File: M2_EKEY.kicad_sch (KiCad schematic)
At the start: 42 parts, among them J2 Bus_M.2_Socket_E, J31 Bus_M.2_Socket_E, J34 Bus_M.2_Socket_E

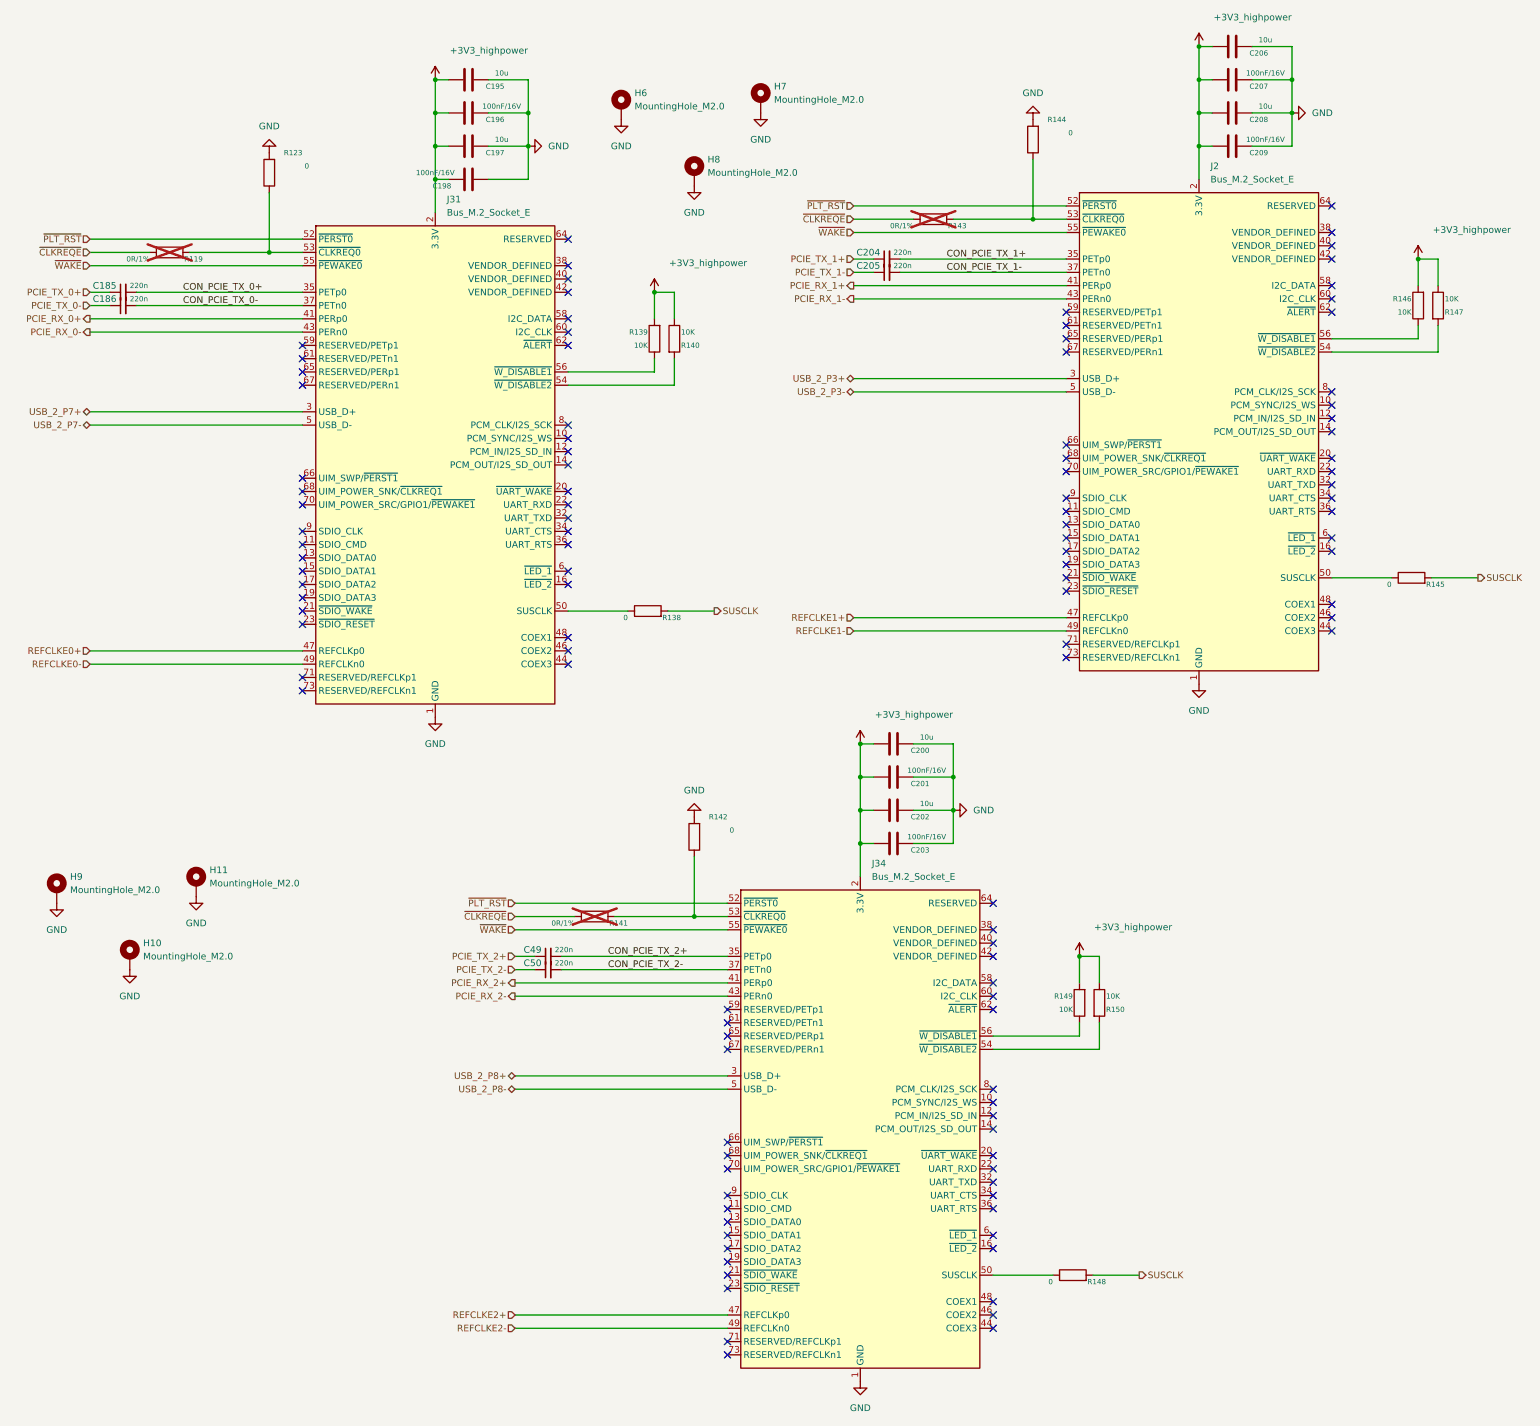
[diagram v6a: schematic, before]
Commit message: added MPN to all parts by hand :'(
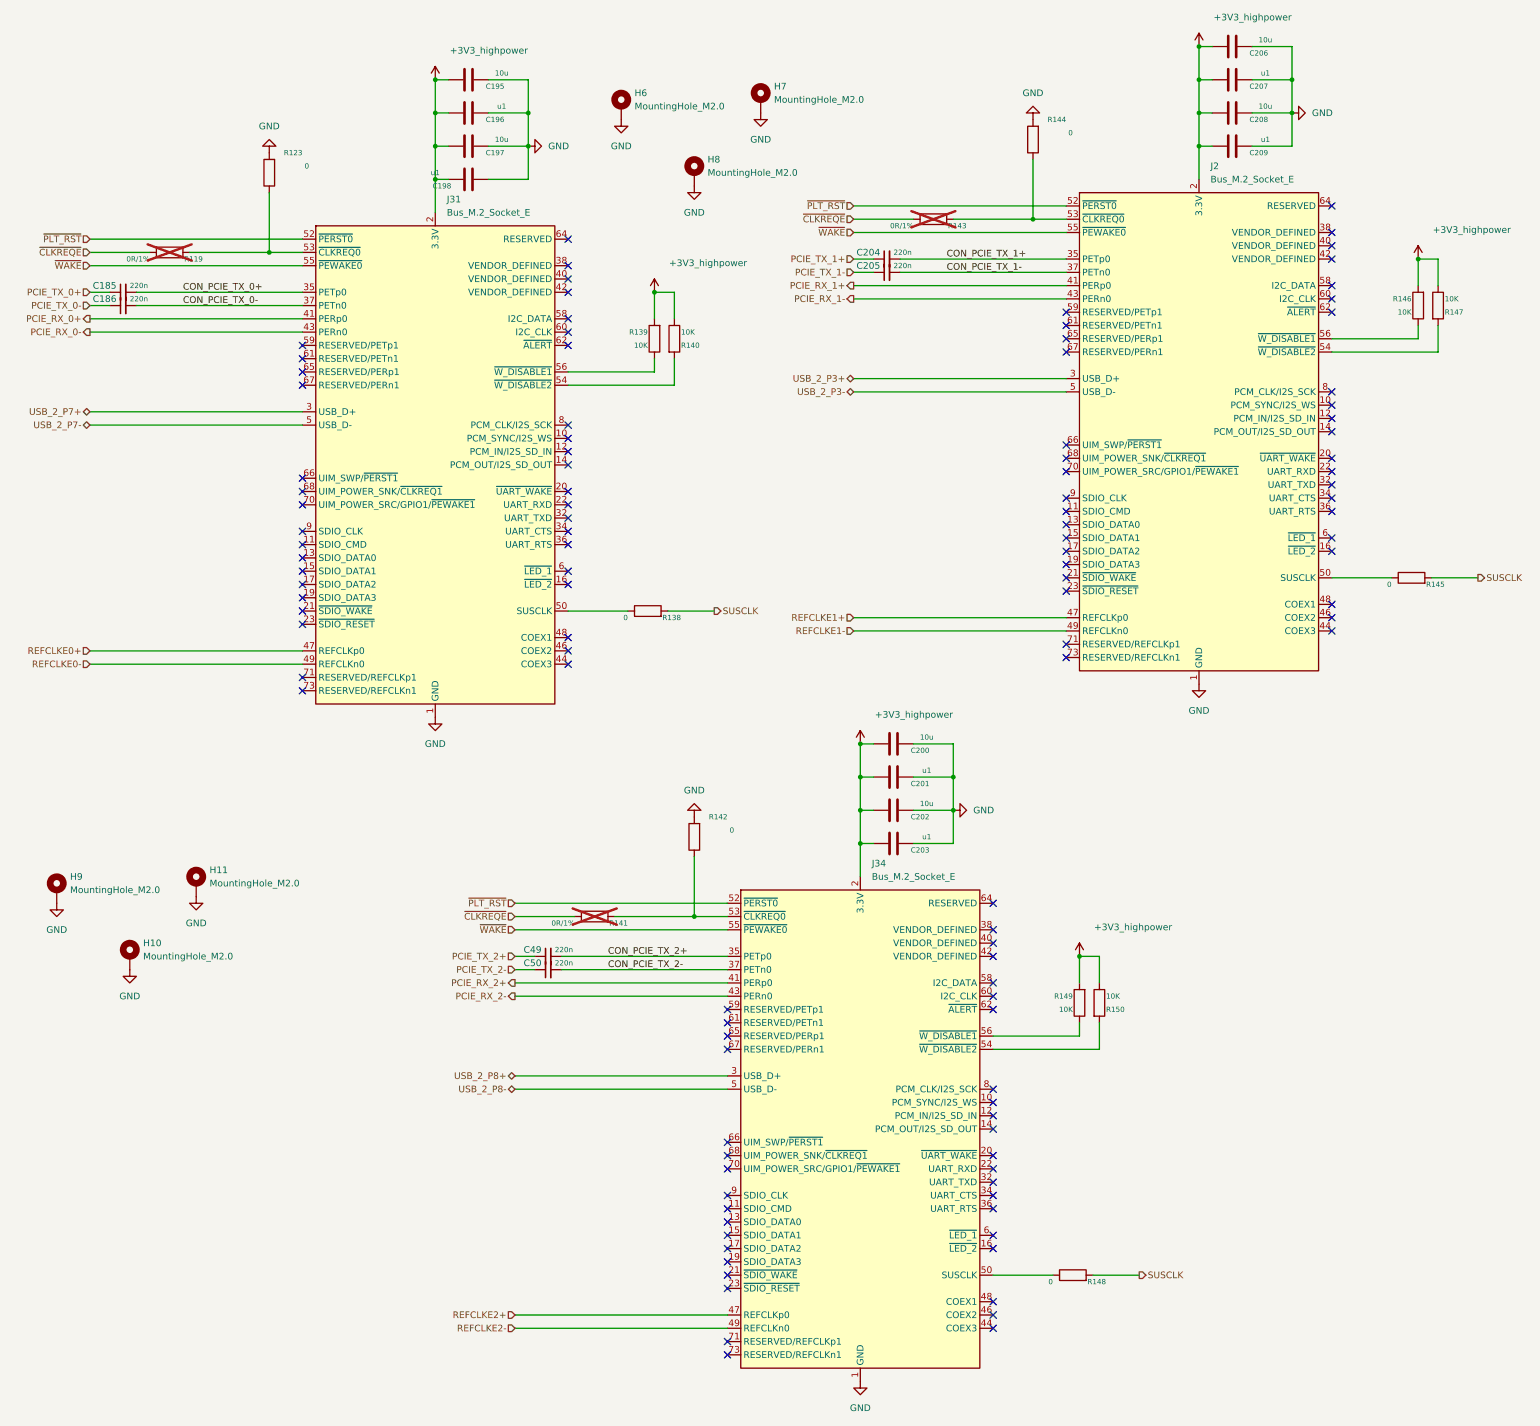
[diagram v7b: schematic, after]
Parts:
- C195, C197, C200, C202, C206, C208: footprint A_HDJ_Library:C_0402_1005Metric -> A_DFRobot:C_0603; DF_Comment 贴片电容0402-10UF-10V-X5R_GRM155R61A106ME44D -> (none); MPN MLASL168BB5106MTNB33 -> GRM188R61E106KA73D; SCH_Show_Footprint C0402 -> (none)
- C196: value 100nF/16V -> u1; MPN (none) -> C1005X7R1H104K050BE
- C198, C201, C203, C207, C209: value 100nF/16V -> u1; DF_Comment 贴片电容0402-100nF-16V-X7R(0402) -> (none); MPN (none) -> C1005X7R1H104K050BE
- J2, J31, J34: MPN (none) -> APCI0108-P001A
- R138, R145, R148: MPN C2889341 -> MCS0402HZ0000ZE100
- R139, R140, R146, R147, R149, R150: MPN RC0402FR-1310KL -> RCS040210K0FKED
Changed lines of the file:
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@@
 			)
 		)
-		(property "Value" "100nF/16V"
+		(property "Value" "u1"
 			(at 229.87 171.45 90)
 			(show_name no)
@@
 			)
 		)
-		(property "Description" ""
+		(property "Description" "16v"
 			(at 223.52 172.72 0)
 			(hide yes)
@@
 			)
 		)
-		(property "DF_Comment" "贴片电容0402-100nF-16V-X7R(0402)"
+		(property "DF_Comment" ""
 			(at 223.52 172.72 0)
 			(hide yes)
@@
 			)
 		)
-		(property "Field-1" ""
+		(property "MPN" "C1005X7R1H104K050BE"
 			(at 223.52 172.72 0)
 			(hide yes)
@@
 			)
 		)
-		(property "Value" "100nF/16V"
+		(property "Value" "u1"
 			(at 294.64 25.4 90)
 			(show_name no)
@@
 			)
 		)
-		(property "DF_Comment" "贴片电容0402-100nF-16V-X7R(0402)"
+		(property "DF_Comment" ""
 			(at 288.29 26.67 0)
 			(hide yes)
@@
 			)
 		)
-		(property "Field-1" ""
+		(property "MPN" "C1005X7R1H104K050BE"
 			(at 288.29 26.67 0)
 			(hide yes)
@@
 			)
 		)
-		(property "Value" "100nF/16V"
+		(property "Value" "u1"
 			(at 294.64 38.1 90)
 			(show_name no)
@@
 			)
 		)
-		(property "DF_Comment" "贴片电容0402-100nF-16V-X7R(0402)"
+		(property "DF_Comment" ""
 			(at 288.29 39.37 0)
 			(hide yes)
@@
 			)
 		)
-		(property "Field-1" ""
+		(property "MPN" "C1005X7R1H104K050BE"
 			(at 288.29 39.37 0)
 			(hide yes)
@@
 			)
 		)
-		(property "Footprint" "A_HDJ_Library:C_0402_1005Metric"
+		(property "Footprint" "A_DFRobot:C_0603"
 			(at 284.48 21.2852 0)
 			(hide yes)
@@
 			)
 		)
-		(property "DF_Comment" "贴片电容0402-10UF-10V-X5R_GRM155R61A106ME44D"
+		(property "DF_Comment" ""
 			(at 288.29 20.32 0)
 			(hide yes)
@@
 			)
 		)
-		(property "SCH_Show_Footprint" "C0402"
+		(property "SCH_Show_Footprint" ""
 			(at 288.29 20.32 0)
 			(hide yes)
@@
 			)
 		)
-		(property "MPN" "MLASL168BB5106MTNB33"
+		(property "MPN" "GRM188R61E106KA73D"
 			(at 288.29 20.32 0)
 			(hide yes)
@@
 			)
 		)
-		(property "Footprint" "A_HDJ_Library:C_0402_1005Metric"
+		(property "Footprint" "A_DFRobot:C_0603"
 			(at 138.43 27.6352 0)
 			(hide yes)
@@
 			)
 		)
-		(property "DF_Comment" "贴片电容0402-10UF-10V-X5R_GRM155R61A106ME44D"
+		(property "DF_Comment" ""
 			(at 142.24 26.67 0)
 			(hide yes)
@@
 			)
 		)
-		(property "SCH_Show_Footprint" "C0402"
+		(property "SCH_Show_Footprint" ""
 			(at 142.24 26.67 0)
 			(hide yes)
@@
 			)
 		)
-		(property "MPN" "MLASL168BB5106MTNB33"
+		(property "MPN" "GRM188R61E106KA73D"
 			(at 142.24 26.67 0)
 			(hide yes)
@@
 			)
 		)
-		(property "MPN" "C2889341"
+		(property "MPN" "MCS0402HZ0000ZE100"
 			(at 322.58 121.92 0)
 			(hide yes)
@@
 			)
 		)
-		(property "Value" "100nF/16V"
+		(property "Value" "u1"
 			(at 229.87 158.75 90)
 			(show_name no)
@@
 			)
 		)
-		(property "DF_Comment" "贴片电容0402-100nF-16V-X7R(0402)"
+		(property "DF_Comment" ""
 			(at 223.52 160.02 0)
 			(hide yes)
@@
 			)
 		)
-		(property "Field-1" ""
+		(property "MPN" "C1005X7R1H104K050BE"
 			(at 223.52 160.02 0)
 			(hide yes)
@@
 			)
 		)
-		(property "MPN" "RC0402FR-1310KL"
+		(property "MPN" "RCS040210K0FKED"
 			(at 323.85 69.85 0)
 			(hide yes)
@@
 			)
 		)
-		(property "Field-1" ""
+		(property "MPN" "APCI0108-P001A"
 			(at 281.94 93.98 0)
 			(hide yes)
@@
 			)
 		)
-		(property "MPN" "C2889341"
+		(property "MPN" "MCS0402HZ0000ZE100"
 			(at 176.53 128.27 0)
 			(hide yes)
@@
 			)
 		)
-		(property "Footprint" "A_HDJ_Library:C_0402_1005Metric"
+		(property "Footprint" "A_DFRobot:C_0603"
 			(at 219.71 154.6352 0)
 			(hide yes)
@@
 			)
 		)
-		(property "DF_Comment" "贴片电容0402-10UF-10V-X5R_GRM155R61A106ME44D"
+		(property "DF_Comment" ""
 			(at 223.52 153.67 0)
 			(hide yes)
@@
 			)
 		)
-		(property "SCH_Show_Footprint" "C0402"
+		(property "SCH_Show_Footprint" ""
 			(at 223.52 153.67 0)
 			(hide yes)
@@
 			)
 		)
-		(property "MPN" "MLASL168BB5106MTNB33"
+		(property "MPN" "GRM188R61E106KA73D"
 			(at 223.52 153.67 0)
 			(hide yes)
@@
 			)
 		)
-		(property "MPN" "C2889341"
+		(property "MPN" "MCS0402HZ0000ZE100"
 			(at 257.81 255.27 0)
 			(hide yes)
@@
 			)
 		)
-		(property "MPN" "RC0402FR-1310KL"
+		(property "MPN" "RCS040210K0FKED"
 			(at 177.8 76.2 0)
 			(hide yes)
@@
 			)
 		)
-		(property "MPN" "RC0402FR-1310KL"
+		(property "MPN" "RCS040210K0FKED"
 			(at 259.08 203.2 0)
 			(hide yes)
@@
 			)
 		)
-		(property "Field-1" ""
+		(property "MPN" "APCI0108-P001A"
 			(at 217.17 227.33 0)
 			(hide yes)
@@
 			)
 		)
-		(property "MPN" "RC0402FR-1310KL"
+		(property "MPN" "RCS040210K0FKED"
 			(at 262.89 203.2 0)
 			(hide yes)
@@
 			)
 		)
-		(property "MPN" "RC0402FR-1310KL"
+		(property "MPN" "RCS040210K0FKED"
 			(at 327.66 69.85 0)
 			(hide yes)
@@
 			)
 		)
-		(property "Field-1" ""
+		(property "MPN" "APCI0108-P001A"
 			(at 135.89 100.33 0)
 			(hide yes)
@@
 			)
 		)
-		(property "Footprint" "A_HDJ_Library:C_0402_1005Metric"
+		(property "Footprint" "A_DFRobot:C_0603"
 			(at 138.43 40.3352 0)
 			(hide yes)
@@
 			)
 		)
-		(property "DF_Comment" "贴片电容0402-10UF-10V-X5R_GRM155R61A106ME44D"
+		(property "DF_Comment" ""
 			(at 142.24 39.37 0)
 			(hide yes)
@@
 			)
 		)
-		(property "SCH_Show_Footprint" "C0402"
+		(property "SCH_Show_Footprint" ""
 			(at 142.24 39.37 0)
 			(hide yes)
@@
 			)
 		)
-		(property "MPN" "MLASL168BB5106MTNB33"
+		(property "MPN" "GRM188R61E106KA73D"
 			(at 142.24 39.37 0)
 			(hide yes)
@@
 			)
 		)
-		(property "Value" "100nF/16V"
+		(property "Value" "u1"
 			(at 135.89 44.45 90)
 			(show_name no)
@@
 			)
 		)
-		(property "DF_Comment" "贴片电容0402-100nF-16V-X7R(0402)"
+		(property "DF_Comment" ""
 			(at 142.24 45.72 0)
 			(hide yes)
@@
 			)
 		)
-		(property "Field-1" ""
+		(property "MPN" "C1005X7R1H104K050BE"
 			(at 142.24 45.72 0)
 			(hide yes)
@@
 			)
 		)
-		(property "Footprint" "A_HDJ_Library:C_0402_1005Metric"
+		(property "Footprint" "A_DFRobot:C_0603"
 			(at 284.48 33.9852 0)
 			(hide yes)
@@
 			)
 		)
-		(property "DF_Comment" "贴片电容0402-10UF-10V-X5R_GRM155R61A106ME44D"
+		(property "DF_Comment" ""
 			(at 288.29 33.02 0)
 			(hide yes)
@@
 			)
 		)
-		(property "SCH_Show_Footprint" "C0402"
+		(property "SCH_Show_Footprint" ""
 			(at 288.29 33.02 0)
 			(hide yes)
@@
 			)
 		)
-		(property "MPN" "MLASL168BB5106MTNB33"
+		(property "MPN" "GRM188R61E106KA73D"
 			(at 288.29 33.02 0)
 			(hide yes)
@@
 			)
 		)
-		(property "Value" "100nF/16V"
+		(property "Value" "u1"
 			(at 148.59 31.75 90)
 			(show_name no)
@@
 			)
 		)
-		(property "Field-1" ""
+		(property "MPN" "C1005X7R1H104K050BE"
 			(at 142.24 33.02 0)
 			(hide yes)
@@
 			)
 		)
-		(property "MPN" "RC0402FR-1310KL"
+		(property "MPN" "RCS040210K0FKED"
 			(at 181.61 76.2 0)
 			(hide yes)
@@
 			)
 		)
-		(property "Footprint" "A_HDJ_Library:C_0402_1005Metric"
+		(property "Footprint" "A_DFRobot:C_0603"
 			(at 219.71 167.3352 0)
 			(hide yes)
@@
 			)
 		)
-		(property "DF_Comment" "贴片电容0402-10UF-10V-X5R_GRM155R61A106ME44D"
+		(property "DF_Comment" ""
 			(at 223.52 166.37 0)
 			(hide yes)
@@
 			)
 		)
-		(property "SCH_Show_Footprint" "C0402"
+		(property "SCH_Show_Footprint" ""
 			(at 223.52 166.37 0)
 			(hide yes)
@@
 			)
 		)
-		(property "MPN" "MLASL168BB5106MTNB33"
+		(property "MPN" "GRM188R61E106KA73D"
 			(at 223.52 166.37 0)
 			(hide yes)
